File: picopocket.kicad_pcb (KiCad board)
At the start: 4 copper layers, 65.6 x 41.4 mm, 88 parts, among them IC1 AR1021, J1 Conn_02x40_Odd_Even, J2 Touchscreen, J3 Audio, Q1 BSS138, Q2 BSS138, U10 74LVC1G08, U11 74LVC1G34, U12 74LVC1G34, U13 74LVC32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

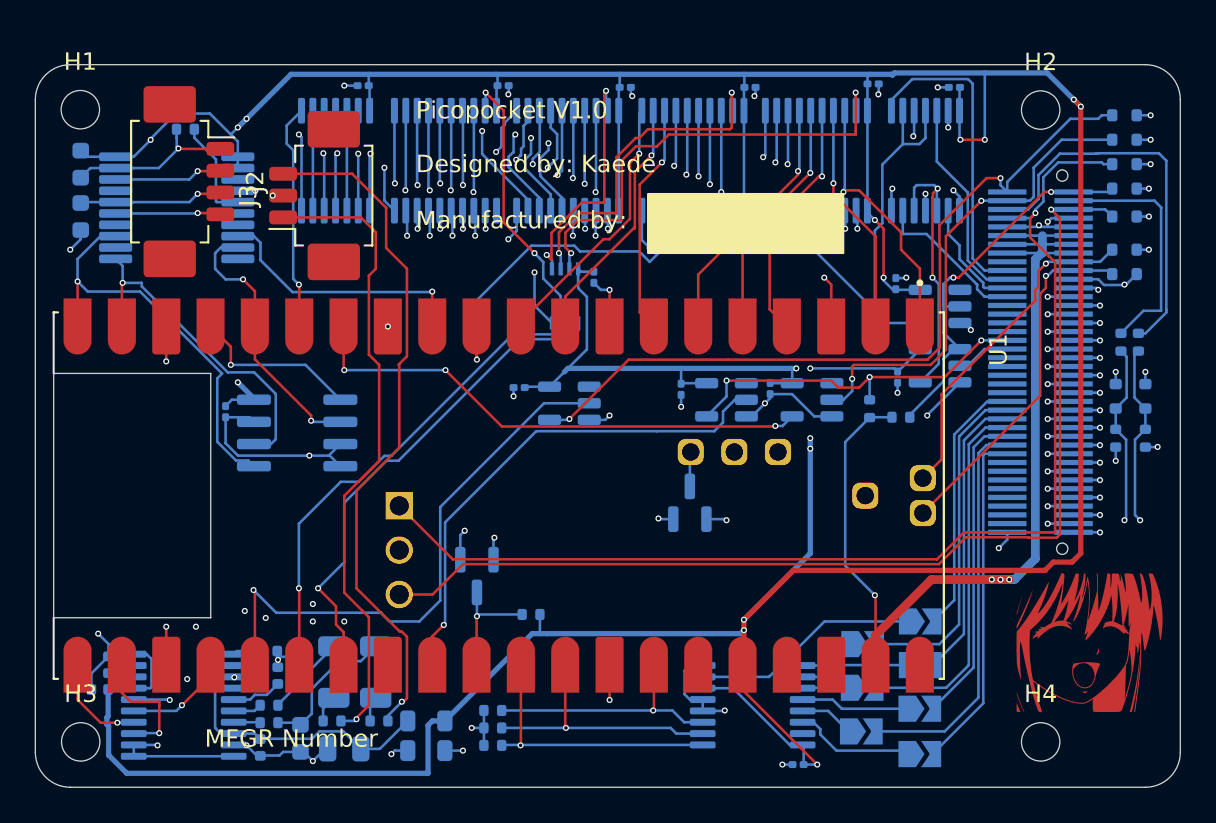
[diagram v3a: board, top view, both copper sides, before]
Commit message: Replace to correct mounting hole, reroute accordingly
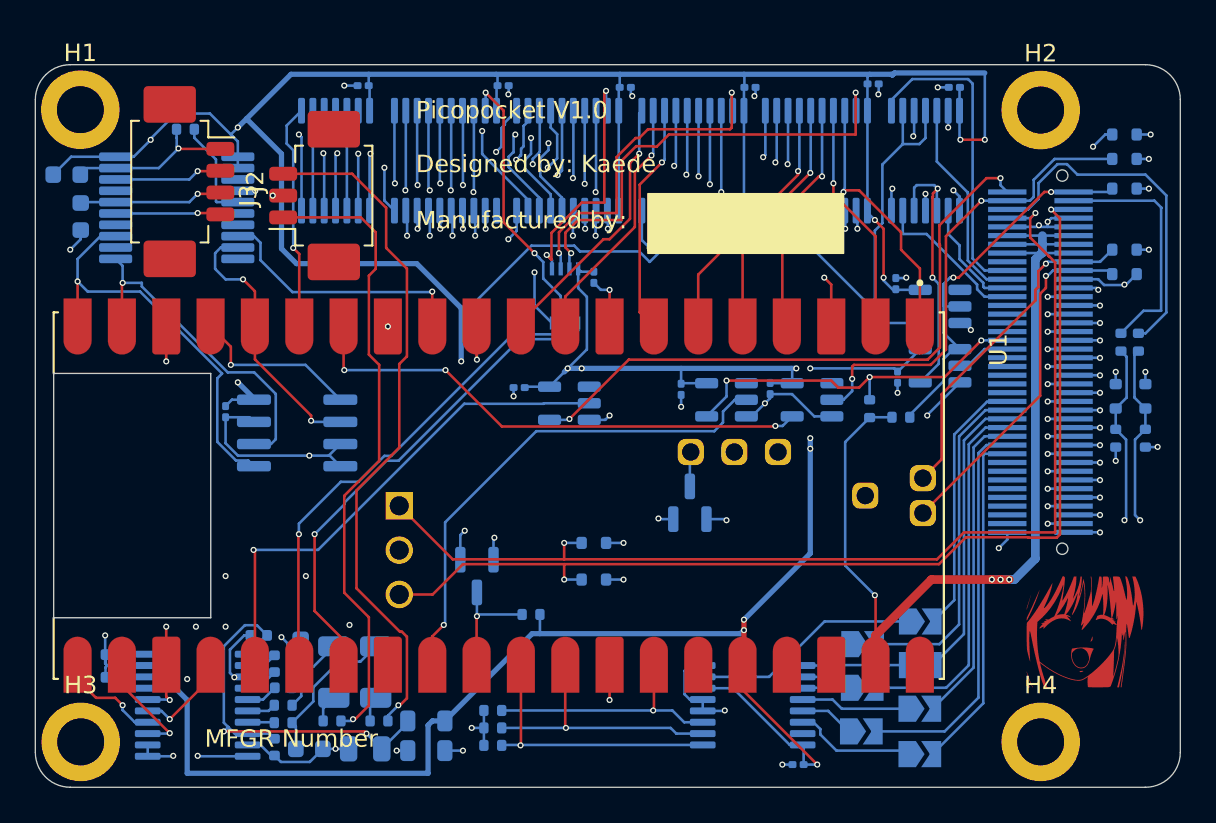
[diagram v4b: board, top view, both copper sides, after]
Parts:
- removed the REF** at (197.5, 124.3)
- added REF**: happyface_smaller, logo:happyface_smaller, F.Cu at (196.8, 122.9)
- H1, H2, H3, H4: footprint MountingHole:MountingHole_2.2mm_M2_ISO7380 -> MountingHole:MountingHole_2.7mm_M2.5_ISO14580_Pad
- moved D4 37.4 mm to (169.0, 112.9)
- moved D3 36.8 mm to (169.0, 115.0)
- moved C3 2.16 mm to (141.5, 119.3)
- moved C6 1.20 mm to (155.9, 124.7)
- moved D7 1.10 mm to (199.4, 90.9)
- moved D9 1.10 mm to (199.4, 89.5)
- moved C5 1.07 mm to (149.8, 118.2), turned to 0 degrees
- moved C7 1.06 mm to (150.7, 119.8)
- moved C10 1.01 mm to (152.2, 119.2)
- moved C1 1.00 mm to (138.8, 91.8), turned to 180 degrees
- moved C4 0.81 mm to (150.7, 124.6)
- moved R6 0.81 mm to (151.2, 122.2)
- moved R7 0.81 mm to (151.2, 123.2)
- moved U16 0.80 mm to (146.3, 122.2)
- moved C11 0.79 mm to (152.7, 124.7), turned to 180 degrees
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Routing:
- net +3.3V: track 287.0 -> 261.9 mm
- net AVDD: track 19.3 -> 24.5 mm, vias 0 -> 2
- net AGND: track 10.1 -> 15.1 mm, vias 6 -> 5
- net GIO7: track 66.8 -> 62.2 mm, vias 1 -> 2
- net R_DRQ: track 32.6 -> 29.3 mm
- net GIO5: track 22.3 -> 20.3 mm
- net GND: track 113.7 -> 115.2 mm
- net Net-(U16-VNEG): track 2.90 -> 1.84 mm
- net BCK: track 7.23 -> 6.33 mm
- net GIO3: track 27.8 -> 27.0 mm
- net DRQ1: track 44.8 -> 44.1 mm, vias 2 -> 3
- net GIO6: track 61.8 -> 61.3 mm, vias 1 -> 2
